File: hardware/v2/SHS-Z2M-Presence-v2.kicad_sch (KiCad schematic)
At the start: 36 parts, among them J1 USB_C_Receptacle, SW1 RESET, SW2 BOOT, U1 ESP32-C6-WROOM-1-N8, U2 LD2410C, U3 LD2450, U4 AP2112K-3.3

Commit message: Fix v2 schematic issues: LEDs, ESD, caps, EN pin, fiducials
- Fix LED1/LED2 rotation for correct pin-wire alignment and polarity
- Fix U4 (AP2112K) EN pin wire — was 5mm misaligned from actual pin
- Change C3/C5/C7 from 0402 to 0805 to avoid 10uF voltage derating
- Add U5 USBLC6-2SC6 for USB ESD protection
- Add FID1-FID3 fiducial markers for SMD assembly
- Remove TP1-TP8 test points and H1-H4 mounting holes (not needed)
- Update DESIGN-NOTES.md with fix status and revised component table

Components reduced from 36 to 28, findings from 44 to 31.

Co-Authored-By: Claude Opus 4.6 <noreply@anthropic.com>
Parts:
- removed H1, H2, H3, H4: MountingHole_M3, MountingHole:MountingHole_3.2mm_M3, symbol SHS-Z2M-Presence-v2:MountingHole
- removed TP1: +5V, TestPoint:TestPoint_Pad_D1.5mm, symbol SHS-Z2M-Presence-v2:TestPoint
- removed TP2: +3V3, TestPoint:TestPoint_Pad_D1.5mm, symbol SHS-Z2M-Presence-v2:TestPoint
- removed TP3: GND, TestPoint:TestPoint_Pad_D1.5mm, symbol SHS-Z2M-Presence-v2:TestPoint
- removed TP4: UART1_TX, TestPoint:TestPoint_Pad_D1.5mm, symbol SHS-Z2M-Presence-v2:TestPoint
- removed TP5: UART1_RX, TestPoint:TestPoint_Pad_D1.5mm, symbol SHS-Z2M-Presence-v2:TestPoint
- removed TP6: UART0_TX, TestPoint:TestPoint_Pad_D1.5mm, symbol SHS-Z2M-Presence-v2:TestPoint
- removed TP7: UART0_RX, TestPoint:TestPoint_Pad_D1.5mm, symbol SHS-Z2M-Presence-v2:TestPoint
- removed TP8: ESP_EN, TestPoint:TestPoint_Pad_D1.5mm, symbol SHS-Z2M-Presence-v2:TestPoint
- added FID1, FID2, FID3: Fiducial, Fiducial:Fiducial_1mm_Dia_2mm_Outer, symbol SHS-Z2M-Presence-v2:Fiducial
- added U5: USBLC6-2SC6, Package_TO_SOT_SMD:SOT-23-6, symbol SHS-Z2M-Presence-v2:USBLC6-2SC6
- C3, C5, C7: footprint Capacitor_SMD:C_0402_1005Metric -> Capacitor_SMD:C_0805_2012Metric
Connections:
- net ESP_EN is gone; now on net +5V: C1.2, C2.2, C3.2, C4.2, C5.2, C6.2, C7.2, C8.1, C8.2, C9.2, J1.A1 (GND), R1.2, R2.2, R3.2, U1.1 (GND), U1.28 (GND), U1.29 (EPAD/GND), U1.3 (EN), U2.4 (GND), U3.4 (GND), U4.2 (GND)
- net +5V: now also LED1.1 (K), LED2.2 (A), U5.2 (GND), U5.5 (VBUS)
- net USB_DM: now also U5.3 (I/O2), U5.4 (I/O2)
- net USB_DP: now also U5.1 (I/O1), U5.6 (I/O1)
- net at R5.2: now also LED1.2 (A)
- net at R6.2: now also LED2.1 (K)
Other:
- moved on the sheet: LED1, LED2

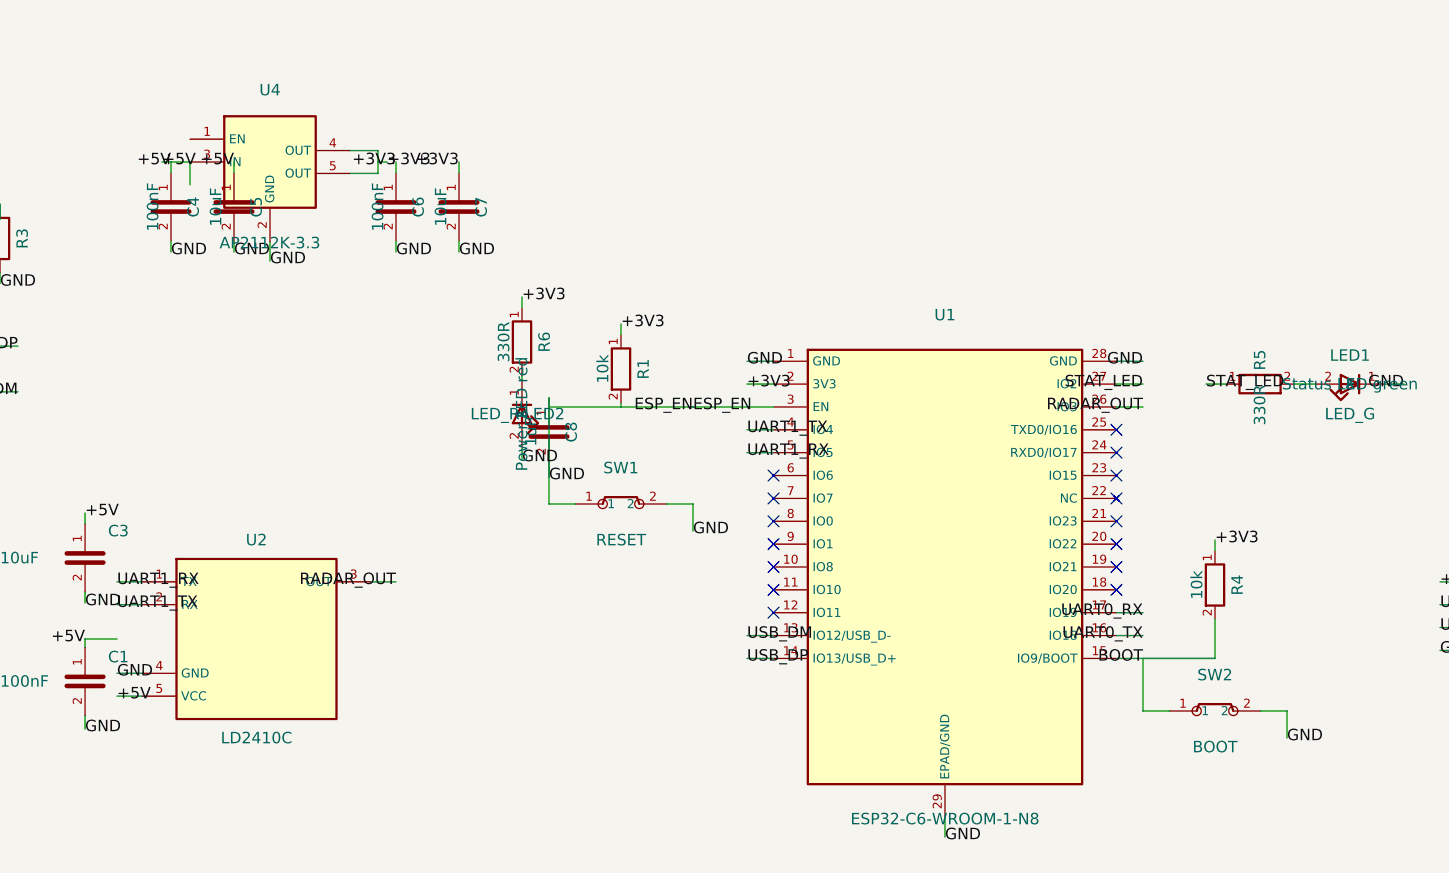
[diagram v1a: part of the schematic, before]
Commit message: Fix schematic wire gaps and restore PCB zone nets
Schematic fixes:
- Fix SW1/SW2 wire endpoints (0.032mm gap: 98.952→98.92, etc.)
  Both switches now correctly connect to ESP_EN/BOOT and GND
- Replace SW1-to-ESP_EN wire through C8 GND area with direct
  ESP_EN label (avoids T-junction short with GND)
- Add direct +5V label on U4.EN wire (avoids T-junction
  dependency through IN pin at same x-coordinate)

PCB fixes:
- Restore zone net assignments stripped during net cleanup:
  F.Cu=GND, B.Cu=GND, In1.Cu=GND, In2.Cu=+3V3

Co-Authored-By: Claude Opus 4.6 <noreply@anthropic.com>
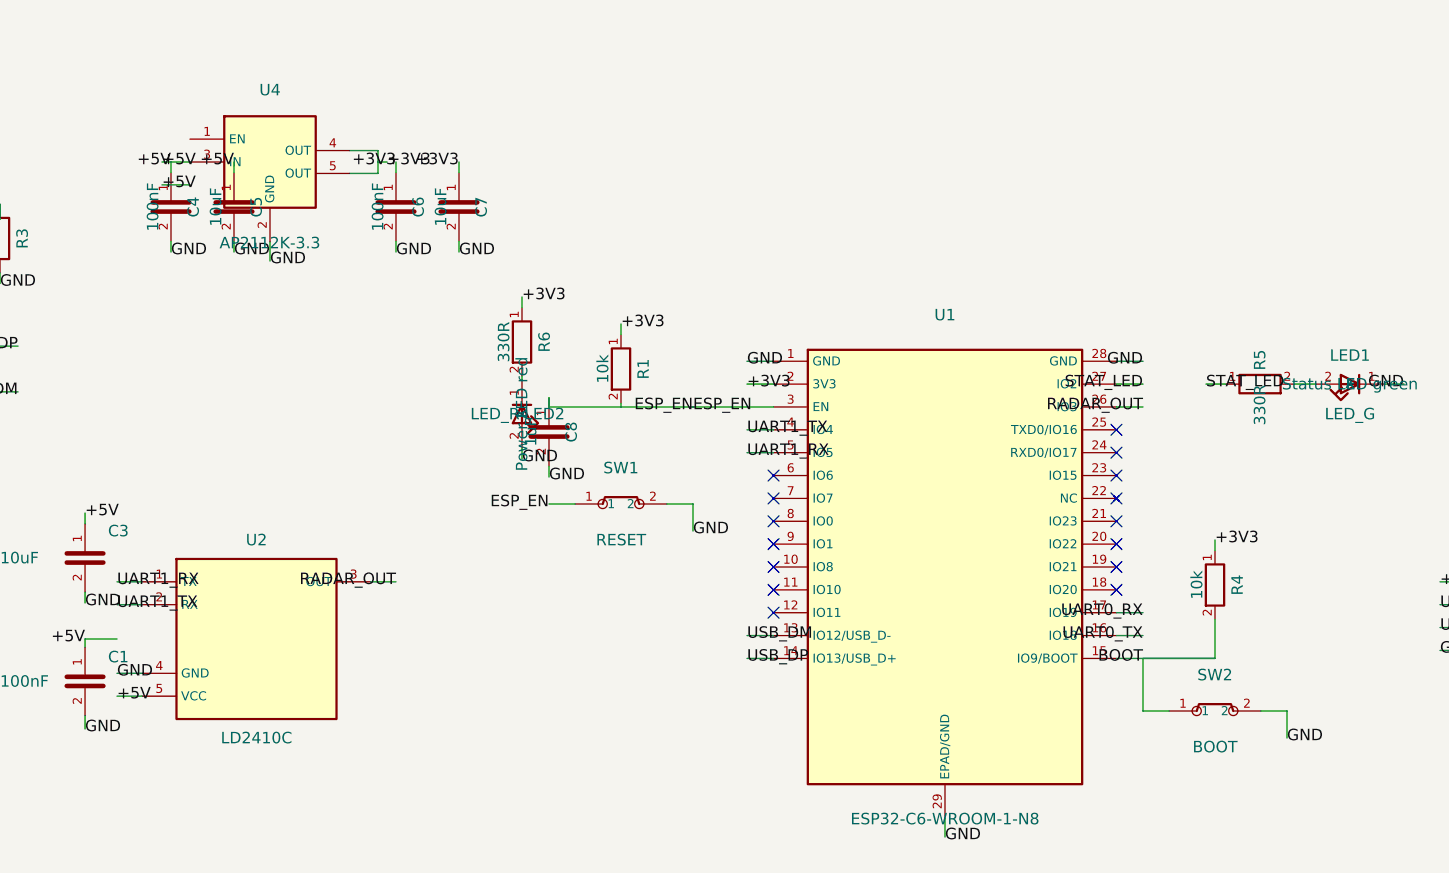
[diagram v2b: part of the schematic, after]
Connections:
- net +5V: now also SW1.2, SW2.2; no longer C8.1, R1.2, U1.3 (EN)
- net BOOT: now also SW2.1
- net ESP_EN: now reaches SW1.1
- net ESP_EN: now also C8.1, R1.2, U1.3 (EN)
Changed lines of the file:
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@@
 		(instances (project "SHS-Z2M-Presence-v2" (path "/b2c3d4e5-0001-0001-0001-000000000001" (reference "U4") (unit 1))))
 	)
-	(wire (pts (xy 56.11 37.54) (xy 56.11 35)) (stroke (width 0) (type default)) (uuid "b2c3d4e5-w020-fix1-0001-000000000001"))
+	(wire (pts (xy 56.11 37.54) (xy 53 37.54)) (stroke (width 0) (type default)) (uuid "b2c3d4e5-w020-fix2-0001-000000000001"))
+	(label "+5V" (at 53 37.54 0) (effects (font (size 1.27 1.27))) (uuid "b2c3d4e5-l010-fix2-0001-000000000001"))
 	(wire (pts (xy 56.11 35) (xy 53 35)) (stroke (width 0) (type default)) (uuid "b2c3d4e5-w021-0001-0001-000000000001"))
 	(label "+5V" (at 53 35 0) (effects (font (size 1.27 1.27))) (uuid "b2c3d4e5-l010-0001-0001-000000000001"))
@@
 		(instances (project "SHS-Z2M-Presence-v2" (path "/b2c3d4e5-0001-0001-0001-000000000001" (reference "SW1") (unit 1))))
 	)
-	(wire (pts (xy 98.952 73) (xy 96 73)) (stroke (width 0) (type default)) (uuid "b2c3d4e5-w404-0001-0001-000000000001"))
-	(wire (pts (xy 96 73) (xy 96 62.22)) (stroke (width 0) (type default)) (uuid "seg0017--w404-0001-0001-000000000001"))
-	(wire (pts (xy 109.048 73) (xy 112 73)) (stroke (width 0) (type default)) (uuid "b2c3d4e5-w405-0001-0001-000000000001"))
+	(wire (pts (xy 98.92 73) (xy 96 73)) (stroke (width 0) (type default)) (uuid "b2c3d4e5-w404-0001-0001-000000000001"))
+	(label "ESP_EN" (at 96 73 180) (effects (font (size 1.27 1.27)) (justify right)) (uuid "b2c3d4e5-l404-fix1-0001-000000000001"))
+	(wire (pts (xy 109.08 73) (xy 112 73)) (stroke (width 0) (type default)) (uuid "b2c3d4e5-w405-0001-0001-000000000001"))
 	(wire (pts (xy 112 73) (xy 112 76)) (stroke (width 0) (type default)) (uuid "seg0019--w405-0001-0001-000000000001"))
 	(label "GND" (at 112 76 0) (effects (font (size 1.27 1.27))) (uuid "b2c3d4e5-l403-0001-0001-000000000001"))
@@
 		(instances (project "SHS-Z2M-Presence-v2" (path "/b2c3d4e5-0001-0001-0001-000000000001" (reference "SW2") (unit 1))))
 	)
-	(wire (pts (xy 164.952 96) (xy 162 96)) (stroke (width 0) (type default)) (uuid "b2c3d4e5-w502-0001-0001-000000000001"))
+	(wire (pts (xy 164.92 96) (xy 162 96)) (stroke (width 0) (type default)) (uuid "b2c3d4e5-w502-0001-0001-000000000001"))
 	(wire (pts (xy 162 96) (xy 162 90.16)) (stroke (width 0) (type default)) (uuid "seg0023--w502-0001-0001-000000000001"))
 	(wire (pts (xy 162 90.16) (xy 170 90.16)) (stroke (width 0) (type default)) (uuid "seg0024--w502-0001-0001-000000000001"))
-	(wire (pts (xy 175.048 96) (xy 178 96)) (stroke (width 0) (type default)) (uuid "b2c3d4e5-w503-0001-0001-000000000001"))
+	(wire (pts (xy 175.08 96) (xy 178 96)) (stroke (width 0) (type default)) (uuid "b2c3d4e5-w503-0001-0001-000000000001"))
 	(wire (pts (xy 178 96) (xy 178 99)) (stroke (width 0) (type default)) (uuid "seg0026--w503-0001-0001-000000000001"))
 	(label "GND" (at 178 99 0) (effects (font (size 1.27 1.27))) (uuid "b2c3d4e5-l501-0001-0001-000000000001"))
